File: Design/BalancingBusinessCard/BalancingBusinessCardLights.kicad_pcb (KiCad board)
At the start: 2 copper layers, 51 x 89 mm, 38 parts, among them J101 Conn_02x01, SW101 SW_Push, U101 ATtiny261A-MU, U401 LIS3DHTR, U402 MCP1640DCH

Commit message: Minor board tweaks
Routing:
- net GND: track 299.2 -> 307.2 mm
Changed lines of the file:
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@@
     (thickness 1.6)
     (drawings 36)
-    (tracks 388)
+    (tracks 386)
     (zones 0)
     (modules 38)
@@
   (segment (start 212.323592 60.967412) (end 212.323592 60.401727) (width 0.4) (layer B.Cu) (net 2))
   (segment (start 214.4 61.4) (end 213.321865 61.4) (width 0.25) (layer B.Cu) (net 2))
-  (segment (start 216.799999 88.599999) (end 216.4 88.2) (width 0.4) (layer B.Cu) (net 2))
-  (segment (start 216.799999 130.307114) (end 216.799999 88.599999) (width 0.4) (layer B.Cu) (net 2))
-  (segment (start 216.45001 130.657103) (end 216.799999 130.307114) (width 0.4) (layer B.Cu) (net 2))
-  (segment (start 214.215071 132.061406) (end 216.45001 130.657103) (width 0.4) (layer B.Cu) (net 2))
-  (segment (start 210.840637 133.242161) (end 214.215071 132.061406) (width 0.4) (layer B.Cu) (net 2))
-  (segment (start 205.5 127.901524) (end 210.840637 133.242161) (width 0.4) (layer B.Cu) (net 2))
-  (segment (start 205.5 116) (end 205.5 127.901524) (width 0.4) (layer B.Cu) (net 2))
+  (segment (start 220.1 133.242161) (end 220.1 91.9) (width 0.4) (layer B.Cu) (net 2))
+  (segment (start 220.1 91.9) (end 216.4 88.2) (width 0.4) (layer B.Cu) (net 2))
+  (segment (start 208.942161 133.242161) (end 220.1 133.242161) (width 0.4) (layer B.Cu) (net 2))
+  (segment (start 205.5 116) (end 205.5 129.8) (width 0.4) (layer B.Cu) (net 2))
+  (segment (start 205.5 129.8) (end 208.942161 133.242161) (width 0.4) (layer B.Cu) (net 2))
   (segment (start 208.75269 74.222184) (end 208.434493 74.540381) (width 0.25) (layer F.Cu) (net 3) (status 20))
   (segment (start 211.777816 74.222184) (end 208.75269 74.222184) (width 0.25) (layer F.Cu) (net 3))

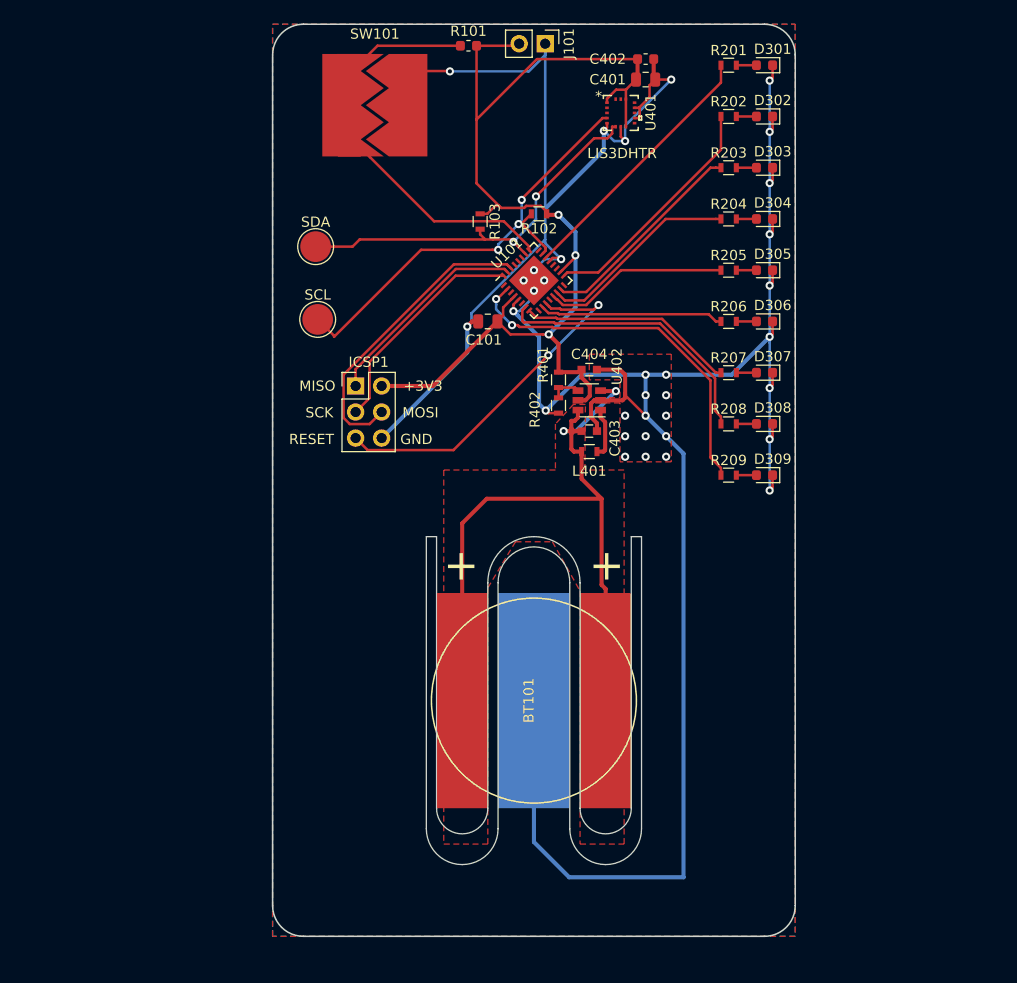
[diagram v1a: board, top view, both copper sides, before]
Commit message: Reverted layout to old one for text placement
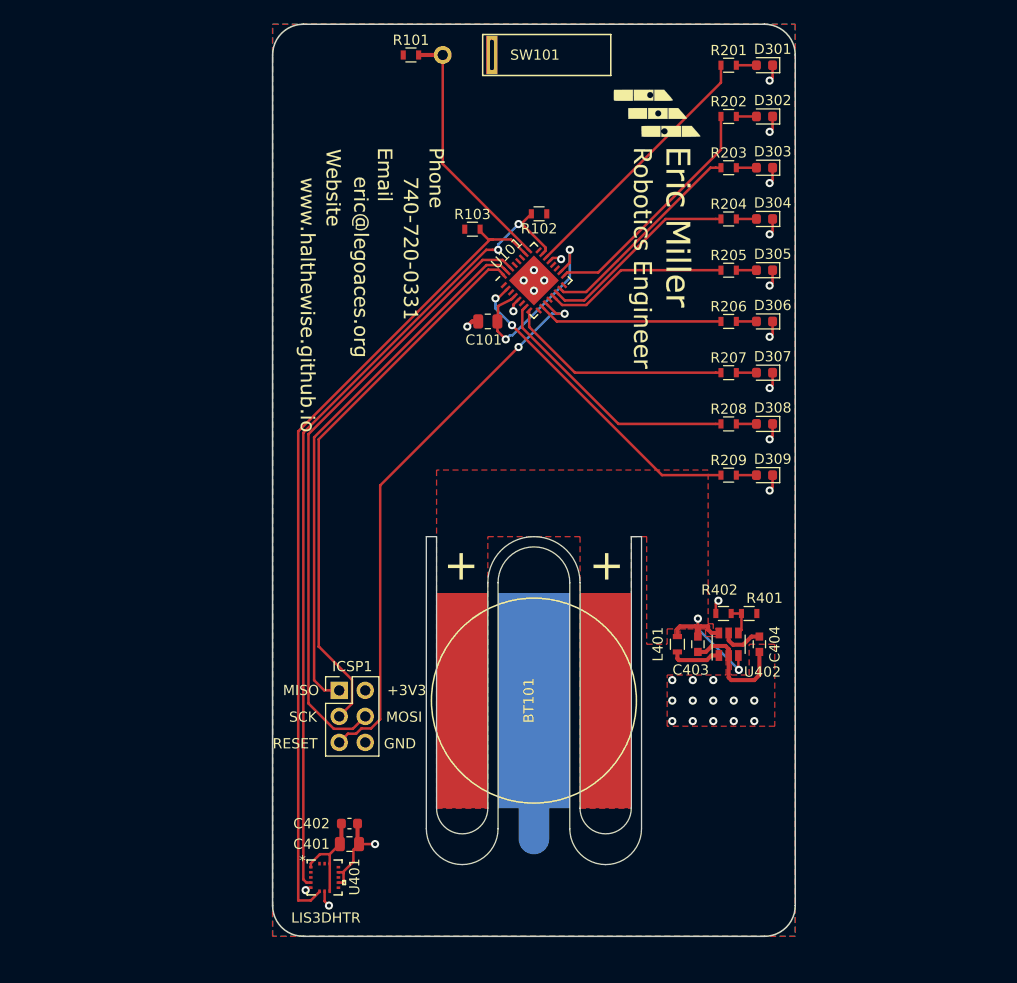
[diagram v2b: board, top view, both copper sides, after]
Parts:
- removed J101: Conn_02x01, Connector_PinHeader_2.54mm:PinHeader_1x02_P2.54mm_Vertical
- removed SCL, SDA: TestPoint, TestPoint:TestPoint_Pad_D3.0mm
- added G***: LOGO, CustomFootprints:EricCardSilkscreen, F.Cu at (205.5, 94.5)
- R101: value 976k -> 10k; footprint Resistor_SMD:R_0603_1608Metric -> Resistors_SMD:R_0603
- SW101: value SW_Push -> SW_SPST; footprint CustomFootprints:TouchButton1 -> CustomFootprints:RB-231X2
- moved C401 80.0 mm to (187.5, 130.0)
- moved C402 80.0 mm to (187.5, 128.0)
- moved U401 80.0 mm to (185.1, 133.3)
- moved C404 31.5 mm to (227.5, 110.5), turned to 270 degrees
- moved ICSP1 29.7 mm to (186.5, 115.0)
- moved R401 29.4 mm to (226.5, 107.5), turned to 180 degrees
- moved U402 27.4 mm to (224.5, 110.5), turned to 90 degrees
- moved R402 25.9 mm to (224.0, 107.5), turned to 180 degrees
- moved C403 23.3 mm to (221.5, 110.5), turned to 270 degrees
- moved L401 20.7 mm to (219.5, 110.5), turned to 90 degrees
- moved SW101 10.3 mm to (199.0, 53.0)
- moved R101 5.68 mm to (193.5, 53.0)
- moved R103 1.06 mm to (199.5, 70.0), turned to 0 degrees
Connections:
- net /LED_0 renamed /DEBUG
- R101 pad 1: /TOUCH -> +3V3
- R101 pad 2: +3V3 -> /TILT
- SW101 pad 1: /TOUCH -> /TILT
- U101 pad 1: (no net) -> Net-(U101-Pad1)
- U101 pad 12: (no net) -> Net-(U101-Pad12)
- U101 pad 16: (no net) -> Net-(U101-Pad16)
- U101 pad 19: (no net) -> Net-(U101-Pad19)
- U101 pad 20: (no net) -> Net-(U101-Pad20)
- U101 pad 24: (no net) -> Net-(U101-Pad24)
- U101 pad 25: /TOUCH -> /TILT
- U101 pad 27: (no net) -> Net-(U101-Pad27)
- U101 pad 28: (no net) -> Net-(U101-Pad28)
- U101 pad 29: (no net) -> Net-(U101-Pad29)
- U101 pad 3: (no net) -> Net-(U101-Pad3)
- U101 pad 6: (no net) -> Net-(U101-Pad6)
- U101 pad 9: (no net) -> Net-(U101-Pad9)
- U401 pad 11: (no net) -> Net-(U401-Pad11)
- U401 pad 13: (no net) -> Net-(U401-Pad13)
- U401 pad 15: (no net) -> Net-(U401-Pad15)
- U401 pad 16: (no net) -> Net-(U401-Pad16)
- U401 pad 2: (no net) -> Net-(U401-Pad2)
- U401 pad 3: (no net) -> Net-(U401-Pad3)
- U401 pad 9: (no net) -> Net-(U401-Pad9)
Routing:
- net GND: track 307.2 -> 56.3 mm, vias 34 -> 33
- net +3V3: track 106.2 -> 33.5 mm, vias 3 -> 2
- net +BATT: track 73.5 -> 16.1 mm
- net /SDA: track 38.9 -> 80.6 mm, vias 2 -> 0
- net /TOUCH: track 41.2 -> 0.00 mm
- net /SCL: track 45.4 -> 80.2 mm, vias 3 -> 2
- net /SCK: track 22.0 -> 54.1 mm
- net /MISO: track 20.6 -> 52.7 mm
- net /MOSI: track 29.6 -> 60.5 mm
- net /TILT: track 0.00 -> 24.9 mm
- net /RESET: track 35.6 -> 55.0 mm
- net /LED_8: track 36.0 -> 31.3 mm
- net /LED_7: track 27.3 -> 25.4 mm
- net /LED_6: track 21.2 -> 22.2 mm

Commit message: Added new components
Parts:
- removed G***: LOGO, CustomFootprints:EricCardSilkscreen
- added J101: Conn_02x01, Connector_PinHeader_2.54mm:PinHeader_1x02_P2.54mm_Vertical, F.Cu at (167.5, 76.2)
- added TP101: TestPoint, TestPoint:TestPoint_Pad_D3.0mm, F.Cu at (167.7, 82.6)
- added TP102: TestPoint, TestPoint:TestPoint_Pad_D3.0mm, F.Cu at (171.3, 76.4)
- C404: footprint Capacitors_SMD:C_0603 -> Capacitor_SMD:C_0805_2012Metric
- R101: value 10k -> 976k; footprint Resistors_SMD:R_0603 -> Resistor_SMD:R_0603_1608Metric
- R102, R103, R201, R202, R203, R204, R205, R206, R207, R208, R209, R401, R402: footprint Resistors_SMD:R_0603 -> Resistor_SMD:R_0603_1608Metric
- SW101: value SW_SPST -> SW_Push; footprint CustomFootprints:RB-231X2 -> CustomFootprints:TouchButton1
- moved SW101 46.7 mm to (160.5, 79.4)
- moved R101 34.7 mm to (170.8, 79.2)
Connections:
- net /DEBUG renamed /LED_0
- R101 pad 1: +3V3 -> /TOUCH
- R101 pad 2: /TILT -> +3V3
- SW101 pad 1: /TILT -> /TOUCH
- U101 pad 1: Net-(U101-Pad1) -> (no net)
- U101 pad 12: Net-(U101-Pad12) -> (no net)
- U101 pad 16: Net-(U101-Pad16) -> (no net)
- U101 pad 19: Net-(U101-Pad19) -> (no net)
- U101 pad 20: Net-(U101-Pad20) -> (no net)
- U101 pad 24: Net-(U101-Pad24) -> (no net)
- U101 pad 25: /TILT -> /TOUCH
- U101 pad 27: Net-(U101-Pad27) -> (no net)
- U101 pad 28: Net-(U101-Pad28) -> (no net)
- U101 pad 29: Net-(U101-Pad29) -> (no net)
- U101 pad 3: Net-(U101-Pad3) -> (no net)
- U101 pad 6: Net-(U101-Pad6) -> (no net)
- U101 pad 9: Net-(U101-Pad9) -> (no net)
- U401 pad 11: Net-(U401-Pad11) -> (no net)
- U401 pad 13: Net-(U401-Pad13) -> (no net)
- U401 pad 15: Net-(U401-Pad15) -> (no net)
- U401 pad 16: Net-(U401-Pad16) -> (no net)
- U401 pad 2: Net-(U401-Pad2) -> (no net)
- U401 pad 3: Net-(U401-Pad3) -> (no net)
- U401 pad 9: Net-(U401-Pad9) -> (no net)
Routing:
- net GND: track 56.3 -> 22.2 mm, vias 33 -> 6
- net /TILT: track 24.9 -> 0.00 mm

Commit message: Fixed .gitignore
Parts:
- removed SW101: SW_Push, CustomFootprints:TouchButton1
- added ?: , CustomButtons:button_v1, F.Cu at (224.7, 134.5)
- added G***: LOGO, CustomFootprints:MaxCardSilkscreen, F.Cu at (210.2, 95.8)
- moved D301 92.7 mm to (187.7, 137.5), turned to 0 degrees
- moved R201 89.9 mm to (191.2, 137.5), turned to 180 degrees
- moved U401 87.8 mm to (230.6, 58.2), turned to 180 degrees
- moved TP101 84.5 mm to (248.0, 108.8), turned to 180 degrees
- moved D302 83.8 mm to (187.7, 132.5), turned to 0 degrees
- moved TP102 82.6 mm to (244.4, 115.0), turned to 180 degrees
- moved R101 82.1 mm to (231.7, 134.3), turned to 270 degrees
- moved R202 80.7 mm to (191.2, 132.5), turned to 180 degrees
- moved C401 79.7 mm to (228.2, 61.5), turned to 180 degrees
- moved C402 76.3 mm to (228.2, 63.5), turned to 180 degrees
- moved D303 75.2 mm to (187.7, 127.5), turned to 0 degrees
- moved R203 71.7 mm to (191.2, 127.5), turned to 180 degrees
- moved D304 67.0 mm to (187.7, 122.5), turned to 0 degrees
- moved R204 63.0 mm to (191.2, 122.5), turned to 180 degrees
- moved J101 62.2 mm to (229.2, 84.1), turned to 270 degrees
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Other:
- outline, holes or cut-outs redrawn

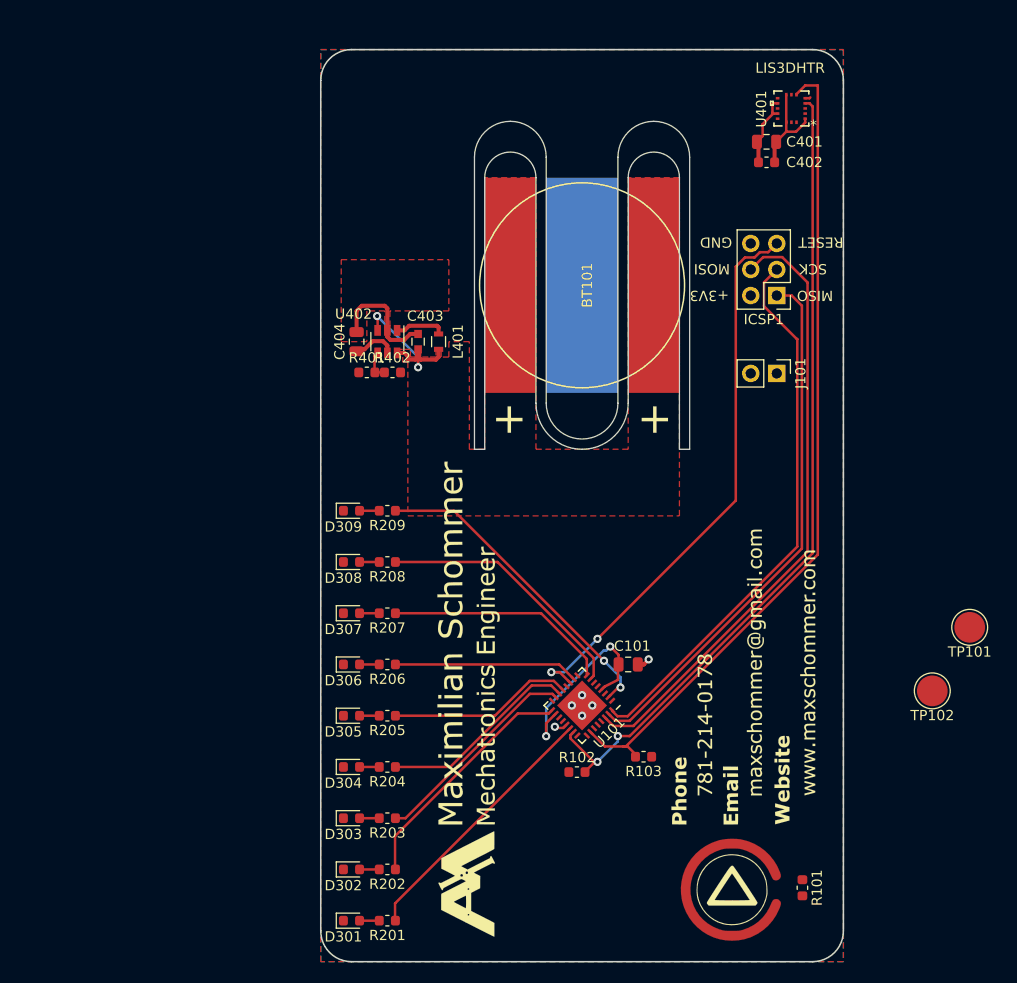
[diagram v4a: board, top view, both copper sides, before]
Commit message: Updated orientation of button
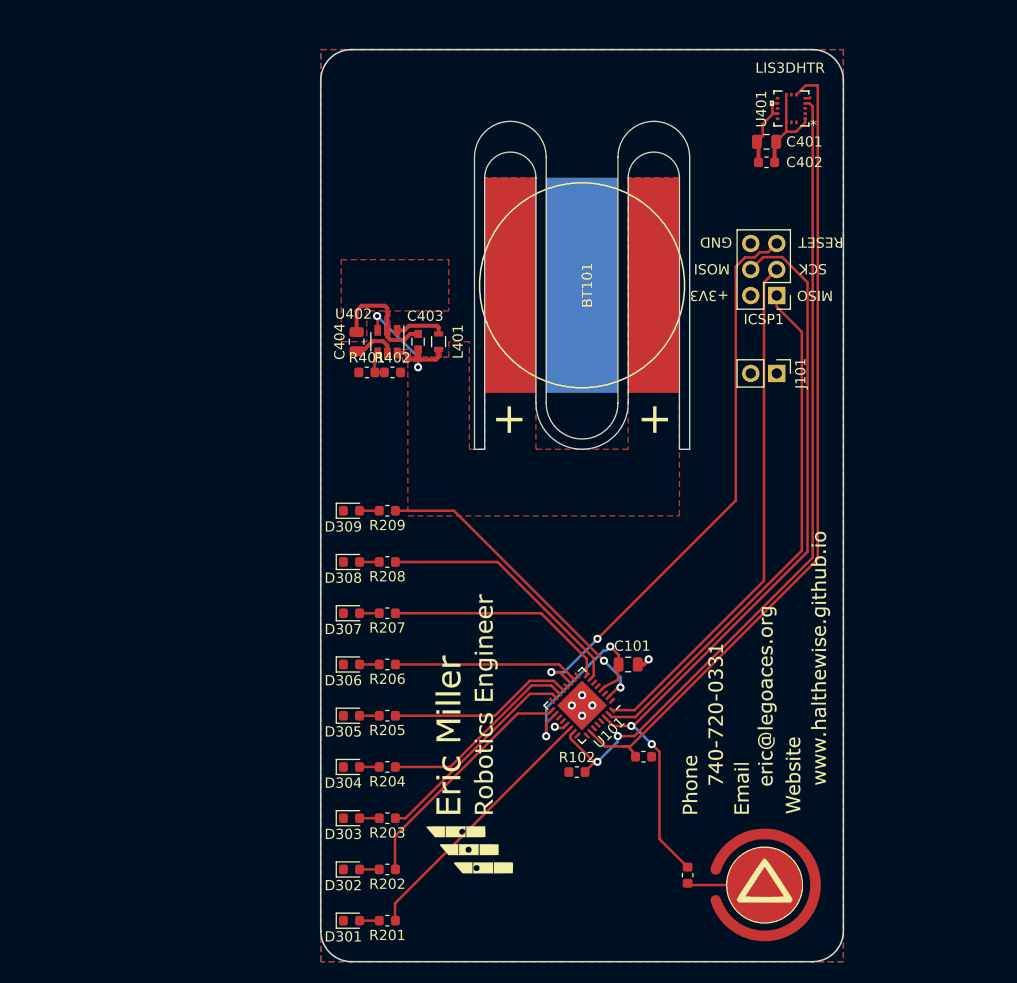
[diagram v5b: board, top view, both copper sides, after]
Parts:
- removed the ? at (224.7, 134.5)
- removed the G*** at (210.2, 95.8)
- removed TP101, TP102: TestPoint, TestPoint:TestPoint_Pad_D3.0mm
- added ?: , CustomFootprints:button_v1, F.Cu at (228.0, 134.0)
- added BTN101: Cap Sense, CustomFootprints:CAP_TOUCH, F.Cu at (228.0, 134.0)
- added G***: LOGO, CustomFootprints:EricCardSilkscreen, F.Cu at (211.2, 94.8)
- moved R101 11.3 mm to (220.5, 133.0), turned to 90 degrees
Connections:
- R101 pad 1: /TOUCH -> /TOUCH_REVEIVE
- R101 pad 2: +3V3 -> /MOSI
- U101 pad 25: /TOUCH -> (no net)
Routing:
- net /MOSI: track 60.5 -> 76.7 mm, vias 0 -> 2
- net /TOUCH_REVEIVE: track 0.00 -> 7.57 mm
- net /SCK: track 54.1 -> 50.9 mm
- net /MISO: track 52.7 -> 51.6 mm

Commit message: Cleaned up fills
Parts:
- removed C403: 4.7uF, Capacitors_SMD:C_0603
- added C2: 22pf, Capacitor_SMD:C_0603_1608Metric, F.Cu at (220.5, 136.3)
- added C5: 4.7uF, Capacitor_SMD:C_0603_1608Metric, F.Cu at (194.2, 81.0)
- added TP1: TestPoint, TestPoint:TestPoint_Pad_D1.0mm, F.Cu at (230.0, 96.2)
- added TP2: TestPoint, TestPoint:TestPoint_Pad_D1.0mm, F.Cu at (230.0, 92.0)
- renumbered BT101 to BT1, BTN101 to BTN1, C101 to C1, C401 to C3, C402 to C4, C404 to C6, D301 to D1, D302 to D2, D303 to D3, D304 to D4, D305 to D5, D306 to D6, D307 to D7, D308 to D8, D309 to D9, J101 to J1, L401 to L1, R102 to R1, R207 to R10, R208 to R11, R209 to R12, R401 to R13, R402 to R14, R103 to R2, R101 to R3, R201 to R4, R202 to R5, R203 to R6, R204 to R7, R205 to R8, R206 to R9, U101 to U1, U401 to U2, U402 to U3
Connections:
- BTN1 pad 1: /TOUCH_REVEIVE -> /TOUCH_RECEIVE
- R3 pad 1: /TOUCH_REVEIVE -> /TOUCH_RECEIVE
- U1 pad 25: (no net) -> /TOUCH_RECEIVE
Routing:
- net GND: track 22.2 -> 309.6 mm, vias 6 -> 30
- net +3V3: track 33.5 -> 151.5 mm, vias 2 -> 3
- net +BATT: track 16.1 -> 82.9 mm
- net /TOUCH_RECEIVE: track 0.00 -> 33.0 mm
- net /TOUCH_REVEIVE: track 7.57 -> 0.00 mm
- net /SDA: track 80.8 -> 85.7 mm
- net /RESET: track 55.0 -> 59.7 mm
- net /SCL: track 80.5 -> 83.6 mm
- net /LED_6: track 22.2 -> 21.2 mm
- net /LED_7: track 25.4 -> 24.6 mm
- net /SCK: track 50.9 -> 51.7 mm
- net /MISO: track 51.6 -> 50.9 mm
- net /LED_8: track 31.3 -> 30.6 mm
